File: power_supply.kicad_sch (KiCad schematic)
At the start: 27 parts, among them J1 USB_C_Receptacle_USB2.0_16P, J2 B2B-XH-A, J3 USB_C_Receptacle_USB2.0_16P, SW9 SW_SPDT

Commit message: feat: connects SPI and I2C pins to MCU
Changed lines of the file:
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@@
 	)
 	(global_label "USB_PROBE_D+"
-		(shape passive)
+		(shape bidirectional)
 		(at 62.23 142.24 0)
 		(fields_autoplaced yes)
@@
 	)
 	(global_label "USB_D-"
-		(shape passive)
+		(shape bidirectional)
 		(at 62.23 72.39 0)
 		(fields_autoplaced yes)
@@
 	)
 	(global_label "USB_D+"
-		(shape passive)
+		(shape bidirectional)
 		(at 62.23 80.01 0)
 		(fields_autoplaced yes)
@@
 	)
 	(global_label "USB_PROBE_D-"
-		(shape passive)
+		(shape bidirectional)
 		(at 62.23 134.62 0)
 		(fields_autoplaced yes)

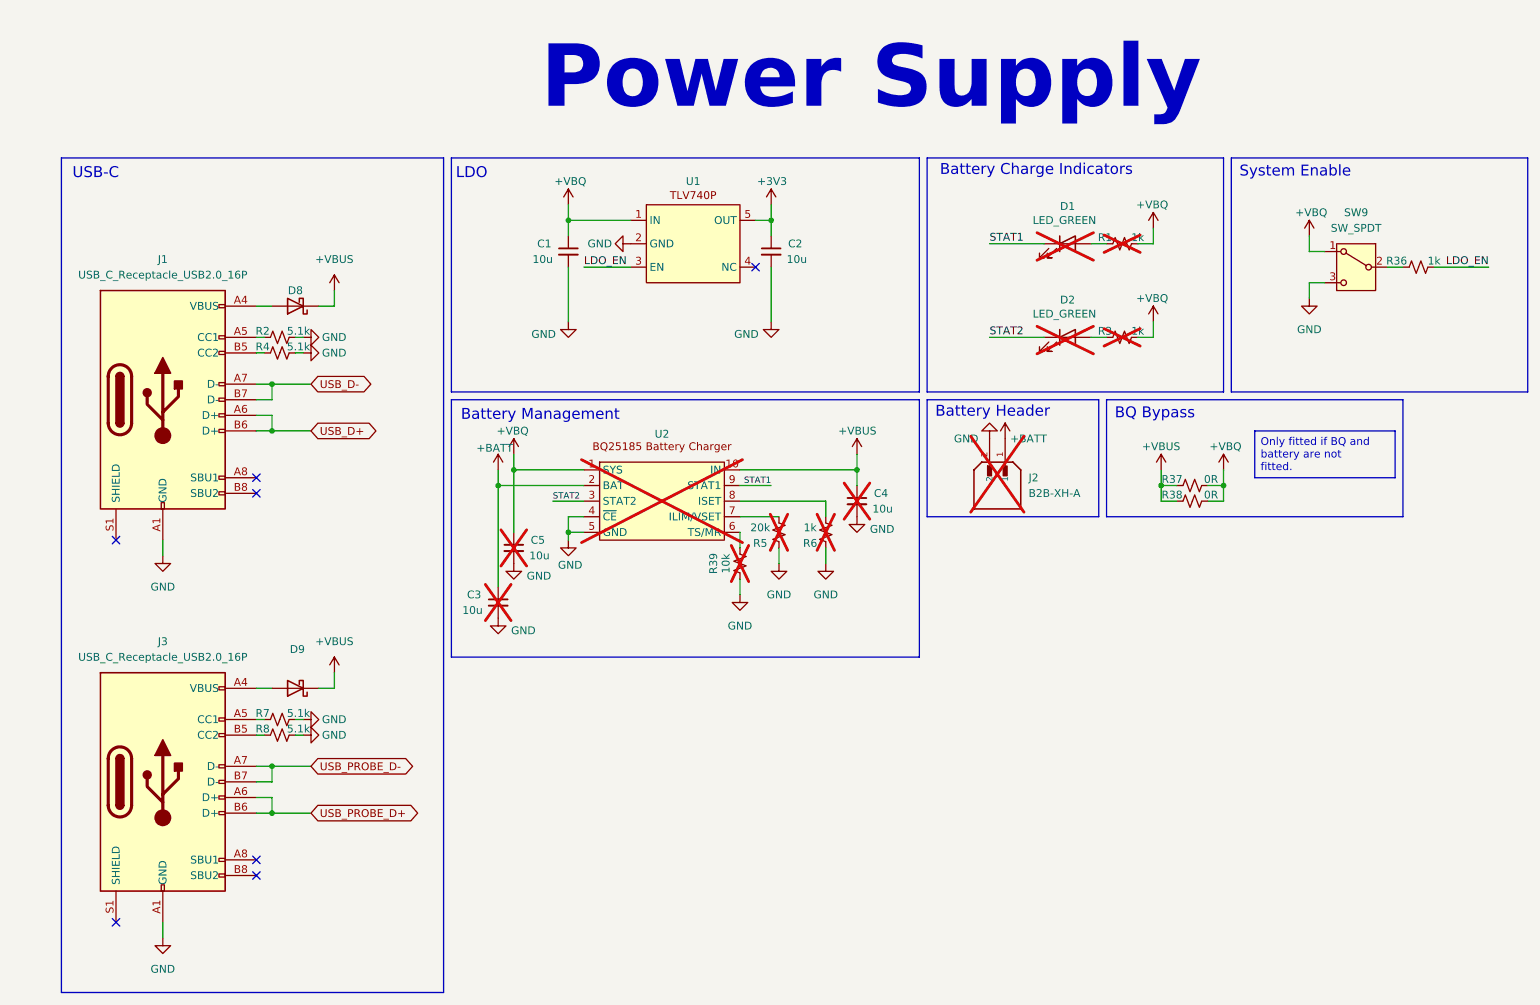
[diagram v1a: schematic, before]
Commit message: feat: adds footprints and new light sensor
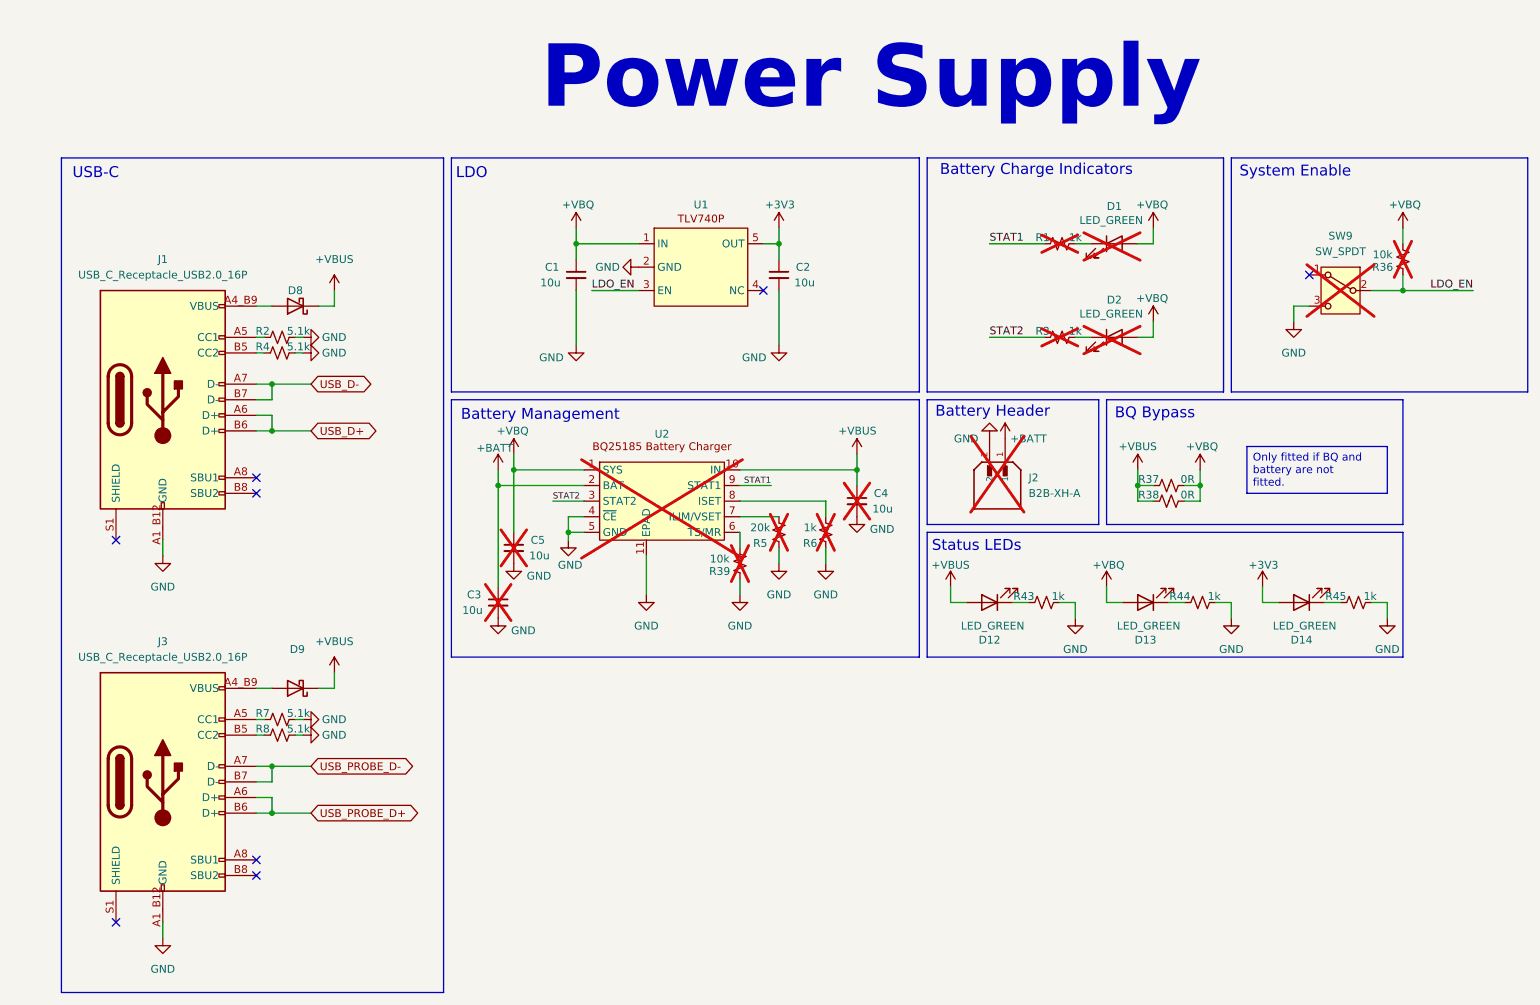
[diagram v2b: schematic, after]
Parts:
- added D12, D13, D14: LED_GREEN, LED_SMD:LED_0603_1608Metric, symbol Device:LED
- added R43, R44, R45: 1k, Resistor_SMD:R_0402_1005Metric, symbol Device:R_Small_US
- J1, J3: footprint (none) -> power_supply:SAMESKY_UJ20-C-H-G-SMT-1-P16-TR
- R36: value 1k -> 10k; MPN RC0402JR-071KL -> RC0402JR-0710KL; now not fitted
- SW9: footprint (none) -> power_supply:SW_SLW-121456-3A-N-D; MPN (none) -> SLW-121456-3A-N-D; now not fitted
- U1: footprint (none) -> power_supply:DBV0005A-IPC_B; MPN (none) -> TLV74033PDBVR
- U2: footprint (none) -> power_supply:WSON10_DLH_TEX; MPN (none) -> BQ25185DLHR
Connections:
- net +3V3: now also D14.2 (A)
- net +VBQ: now also D1.2 (A), D2.2 (A), R36.2, D13.2 (A); no longer R1.2, R3.2, SW9.1 (A)
- net +VBUS: now also D12.2 (A)
- net GND: now also J1.A1_B12 (GND), J1.B1_A12 (GND), J3.A1_B12 (GND), J3.B1_A12 (GND), U2.11 (EPAD), R43.1, R44.1, R45.1; no longer J1.A1 (GND), J1.A12 (GND), J1.B1 (GND), J1.B12 (GND), J3.A1 (GND), J3.A12 (GND), J3.B1 (GND), J3.B12 (GND)
- net LDO_EN: now also SW9.2 (B)
- net STAT1: now also R1.1; no longer D1.1 (K)
- net STAT2: now also R3.1; no longer D2.1 (K)
- new net: D12.1 (K), R43.2
- new net: D13.1 (K), R44.2
- new net: D1.1 (K), R1.2
- new net: D9.2 (A), J3.A4_B9 (VBUS), J3.B4_A9 (VBUS)
- new net: D2.1 (K), R3.2
- new net: D14.1 (K), R45.2
- new net: D8.2 (A), J1.A4_B9 (VBUS), J1.B4_A9 (VBUS)
- no-connect marks 7 -> 8
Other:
- note added: "Status LEDs"
- moved on the sheet: C1, C2, D1, D2, J1, J3, R1, R3, R37, R38, U1

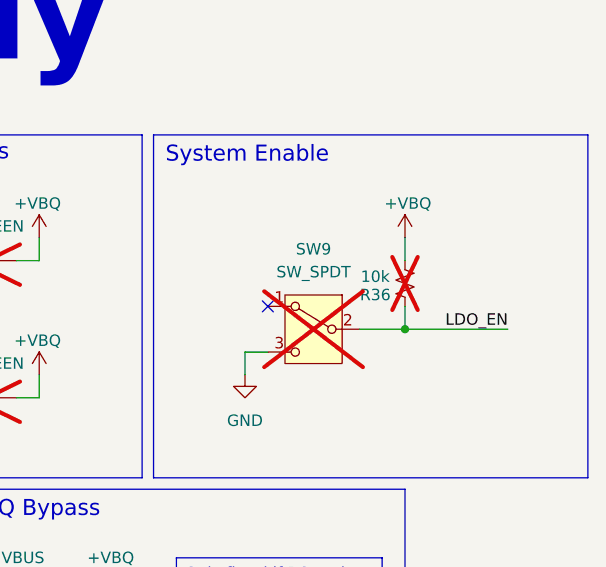
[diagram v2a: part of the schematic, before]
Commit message: feat: connects all global labels
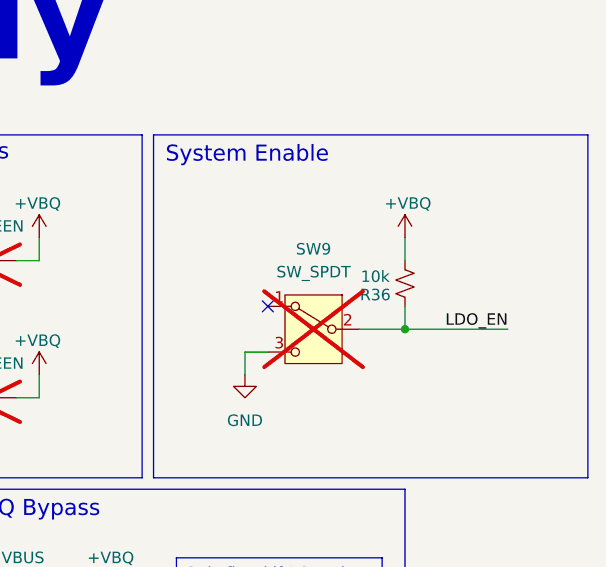
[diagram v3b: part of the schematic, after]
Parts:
- R36: now fitted
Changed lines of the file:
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@@
 		(in_bom yes)
 		(on_board yes)
-		(dnp yes)
+		(dnp no)
 		(property "Reference" "R36"
 			(at 236.728 53.34 0)

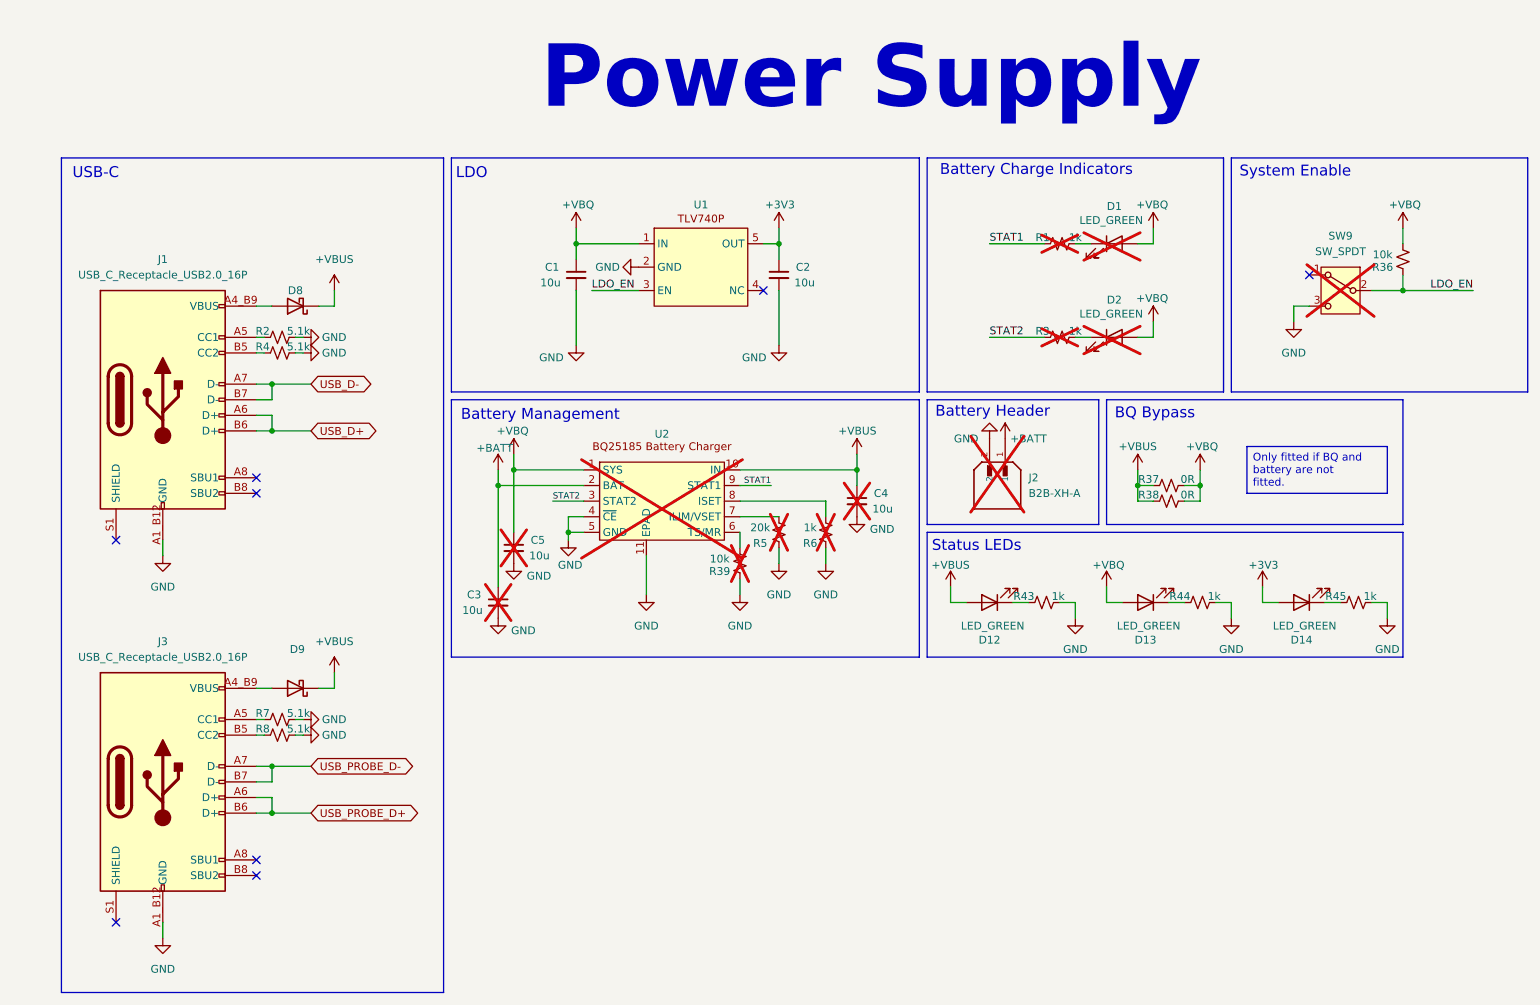
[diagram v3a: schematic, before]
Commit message: chore: makes changes for DRC check compliance
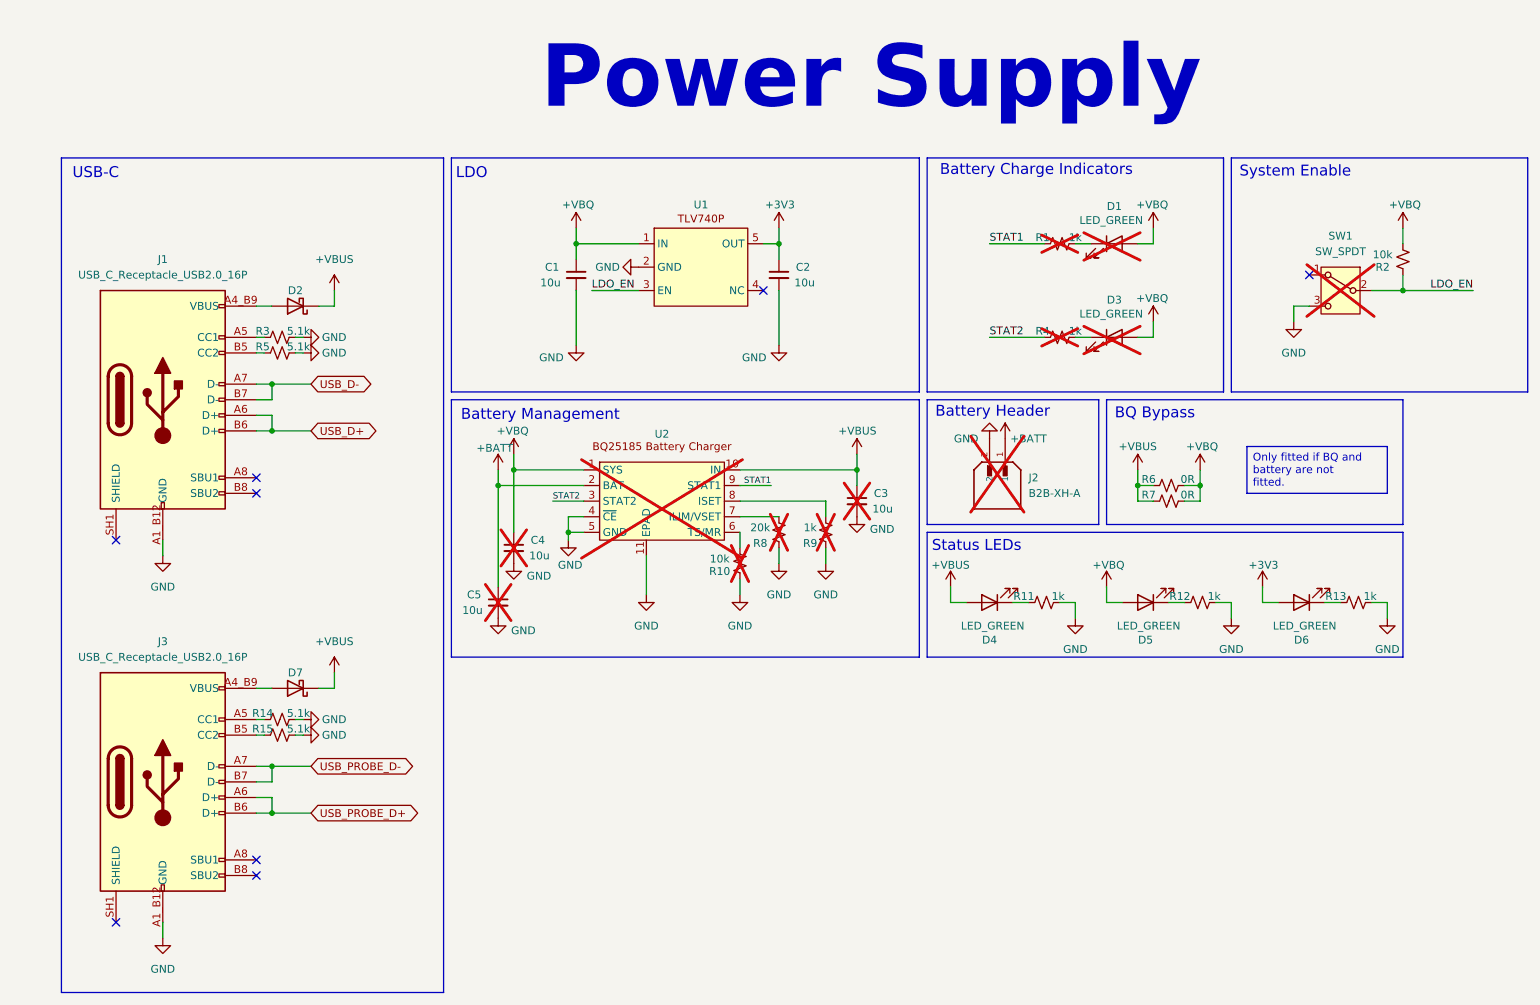
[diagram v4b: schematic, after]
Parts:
- removed D9: D_Schottky, symbol Device:D_Schottky
- added D7: D_Schottky, Diode_SMD:D_SOD-123F, symbol Device:D_Schottky
- D2: renamed from D8; footprint (none) -> Diode_SMD:D_SOD-123F
- renumbered C4 to C3, C5 to C4, C3 to C5, D2 to D3, D12 to D4, D13 to D5, D14 to D6, R39 to R10, R43 to R11, R44 to R12, R45 to R13, R7 to R14, R8 to R15, R36 to R2, R2 to R3, R3 to R4, R4 to R5, R37 to R6, R38 to R7, R5 to R8, R6 to R9, SW9 to SW1
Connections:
- net +VBUS: now also D7.1 (K)
- net at J3.A4_B9 (VBUS), J3.B4_A9 (VBUS): now also D7.2 (A)
- new net: J1.SH1 (SHIELD), J1.SH2 (SHIELD), J1.SH3 (SHIELD), J1.SH4 (SHIELD)
- new net: J3.SH1 (SHIELD), J3.SH2 (SHIELD), J3.SH3 (SHIELD), J3.SH4 (SHIELD)

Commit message: feat: adds testpoints
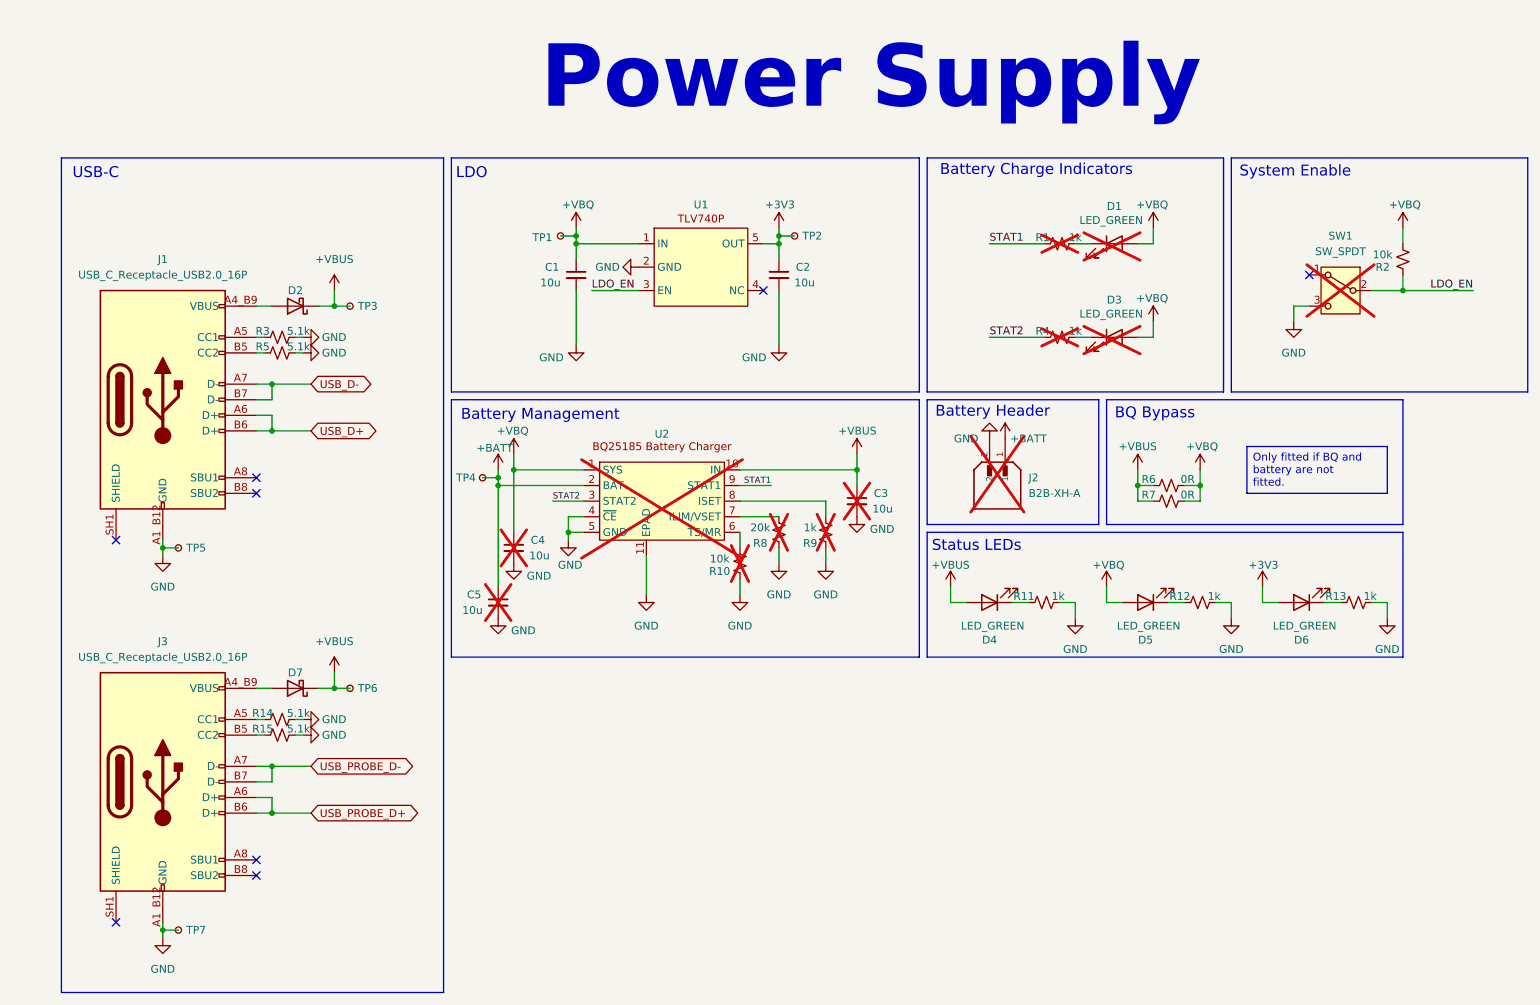
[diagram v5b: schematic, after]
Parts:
- added TP1, TP2, TP3, TP4, TP5, TP6, TP7: TestPoint_Small, TestPoint:TestPoint_Pad_D1.0mm, symbol Connector:TestPoint_Small
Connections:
- net +3V3: now also TP2.1
- net +BATT: now also TP4.1
- net +VBQ: now also TP1.1
- net +VBUS: now also TP3.1, TP6.1
- net GND: now also TP5.1, TP7.1
